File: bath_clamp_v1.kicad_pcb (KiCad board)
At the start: 6 copper layers, 70.9 x 62 mm, 31 parts, among them J1 105-1103-001, J2 105-1103-001, K1 1462042-8, K2 1462042-8, Q1 MBT3904DW1T1G, Q2 MBT3904DW1T1G, Q3 MBT3904DW1T1G, U1 OPA828, U17 MAX5802, U2 ADG1208, U3 G6L-1F-TR-DC5, U4 G6L-1F-TR-DC5, U5 G6L-1F-TR-DC5

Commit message: updates to pcb layout
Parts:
- removed C52, C53: 0.1u, bath_clamp_v1:C0603
- removed H2, H4: MOUNT-HOLE3.0, bath_clamp_v1:3,0
- removed Q2: MBT3904DW1T1G, digikey-footprints:SOT-363
- removed U$1, U$2: HDMI, bath_clamp_v1:HDMI_A
- added C10: 200pF, Capacitor_SMD:C_0603_1608Metric, F.Cu at (113.0, 73.0)
- added C11: 1nF, Capacitor_SMD:C_0603_1608Metric, F.Cu at (113.0, 73.0)
- added C12: 4.7nF, Capacitor_SMD:C_0603_1608Metric, F.Cu at (113.0, 73.0)
- added C13: 0.1u, Capacitor_SMD:C_0603_1608Metric, F.Cu at (62.0, 74.0)
- added C14, C18, C5, C7: 0.1u, Capacitor_SMD:C_0603_1608Metric, F.Cu at (113.0, 73.0)
- added C15: 4.7u, Capacitor_SMD:C_1206_3216Metric, F.Cu at (52.0, 74.0)
- added C16: 4.7u, Capacitor_SMD:C_1206_3216Metric, F.Cu at (61.0, 66.0)
- added C17: 0.1u, Capacitor_SMD:C_0603_1608Metric, F.Cu at (56.0, 59.0)
- added C19: 2.2u, Capacitor_SMD:C_0603_1608Metric, F.Cu at (113.0, 73.0)
- added C2: 0.1u, Capacitor_SMD:C_0603_1608Metric, F.Cu at (47.0, 74.0)
- added C20: 0.1u, Capacitor_SMD:C_0603_1608Metric, F.Cu at (107.0, 8.00)
- added C21: 0.1u, Capacitor_SMD:C_0603_1608Metric, F.Cu at (51.0, 59.0)
- added C22: 0.1u, Capacitor_SMD:C_0603_1608Metric, F.Cu at (57.0, 74.0)
- added C23: DNI, Capacitor_SMD:C_0603_1608Metric, F.Cu at (119.0, 13.0)
- added C24: DNI, Capacitor_SMD:C_0603_1608Metric, F.Cu at (113.0, 73.0)
- added C25: DNI, Capacitor_SMD:C_0603_1608Metric, F.Cu at (124.0, 10.0)
- added C26: DNI, Capacitor_SMD:C_0603_1608Metric, F.Cu at (119.0, 9.00)
- added C3: 1u, Capacitor_SMD:C_0603_1608Metric, F.Cu at (42.0, 74.0)
- added C4: 0.1u, Capacitor_SMD:C_0603_1608Metric, F.Cu at (112.0, 8.00)
- added C6: 4.7n, Capacitor_SMD:C_0603_1608Metric, F.Cu at (113.0, 73.0)
- added C8: 0.1u, Capacitor_SMD:C_0603_1608Metric, F.Cu at (61.0, 59.0)
- added C9: 47pF, Capacitor_SMD:C_0603_1608Metric, F.Cu at (113.0, 73.0)
- added H5: MountingHole_Pad, MountingHole:MountingHole_3.2mm_M3_DIN965_Pad, F.Cu at (55.0, 66.0)
- added H7: MountingHole_Pad, MountingHole:MountingHole_3.2mm_M3_DIN965_Pad, F.Cu at (92.0, 17.0)
- added IC1: DAC53401DSGR, covg-kicad:SON50P200X200X80-9N, F.Cu at (124.0, 37.0)
- added J3: 105-1103-001, digikey-footprints:Test_Jack_Horiz, F.Cu at (123.0, 25.0)
- added Q4: MBT3904DW1T1G, digikey-footprints:SOT-363, F.Cu at (112.0, 26.0)
- added R1, R23, R26: 0, Resistor_SMD:R_0603_1608Metric, F.Cu at (113.0, 73.0)
- added R10, R11, R12, R13, R19, R2, R22, R27, R31, R38, R50, R9: 10k, Resistor_SMD:R_0603_1608Metric, F.Cu at (113.0, 73.0)
- added R14, R15, R16: 240, Resistor_SMD:R_0603_1608Metric, F.Cu at (113.0, 73.0)
- added R17: 1.13k, Resistor_SMD:R_0603_1608Metric, F.Cu at (113.0, 73.0)
- added R18, R24, R44, R45: 33, Resistor_SMD:R_0603_1608Metric, F.Cu at (113.0, 73.0)
- added R20: 73.2k, Resistor_SMD:R_0603_1608Metric, F.Cu at (45.0, 66.0)
- added R21: 73.2k, Resistor_SMD:R_0603_1608Metric, F.Cu at (45.0, 70.0)
- added R25, R30: 20k, Resistor_SMD:R_0603_1608Metric, F.Cu at (113.0, 73.0)
- added R28, R29: 73.2k, Resistor_SMD:R_0603_1608Metric, F.Cu at (113.0, 73.0)
- added R3, R47: 33.2k, Resistor_SMD:R_0603_1608Metric, F.Cu at (113.0, 73.0)
- added R32: 12.1k, Resistor_SMD:R_0603_1608Metric, F.Cu at (113.0, 73.0)
- added R37: 2.49k, Resistor_SMD:R_0603_1608Metric, F.Cu at (113.0, 73.0)
- added R39, R40: 1820, Resistor_SMD:R_0603_1608Metric, F.Cu at (113.0, 73.0)
- added R4: 100k, Resistor_SMD:R_0603_1608Metric, F.Cu at (113.0, 73.0)
- added R41: 1k, Resistor_SMD:R_0603_1608Metric, F.Cu at (113.0, 73.0)
- added R42, R43: 499, Resistor_SMD:R_0603_1608Metric, F.Cu at (113.0, 73.0)
- added R46: 3.01k, Resistor_SMD:R_0603_1608Metric, F.Cu at (113.0, 73.0)
- added R48: 27.4k, Resistor_SMD:R_0603_1608Metric, F.Cu at (113.0, 73.0)
- added R49: 3.01k, Resistor_SMD:R_0603_1608Metric, F.Cu at (124.0, 14.0)
- added R5: 332k, Resistor_SMD:R_0603_1608Metric, F.Cu at (113.0, 73.0)
- added R51: DNI, Resistor_SMD:R_0603_1608Metric, F.Cu at (113.0, 73.0)
- added R6: 1M, Resistor_SMD:R_0603_1608Metric, F.Cu at (113.0, 73.0)
- added R7: 3.32M, Resistor_SMD:R_0603_1608Metric, F.Cu at (113.0, 73.0)
- added R8: 10M, Resistor_SMD:R_0603_1608Metric, F.Cu at (113.0, 73.0)
- added U10: LP2951-3.3_SOIC, Package_SO:SOIC-8_3.9x4.9mm_P1.27mm, F.Cu at (81.0, 64.0)
- added U11: AD8615, Package_TO_SOT_SMD:TSOT-23-5, F.Cu at (124.0, 42.0)
- added U12: TCA9555DBR, Package_SO:SSOP-24_5.3x8.2mm_P0.65mm, F.Cu at (113.0, 63.0)
- added U13: TCA9555DBR, Package_SO:SSOP-24_5.3x8.2mm_P0.65mm, F.Cu at (116.0, 51.0)
- added U14: DG412xUE, Package_SO:TSSOP-16_4.4x5mm_P0.65mm, F.Cu at (117.0, 41.0)
- added U15: OPA828, Package_SO:SOIC-8_3.9x4.9mm_P1.27mm, F.Cu at (113.0, 73.0)
- added U16: TMUX6111PWR, Package_SO:TSSOP-16_4.4x5mm_P0.65mm, F.Cu at (92.0, 70.0)
- added U18: AD8421ARZ, digikey-footprints:TSSOP-8_W3mm, F.Cu at (70.0, 65.0)
- added U19: ADA4932-1YCPZ-R7, digikey-footprints:VFQFN-16-1EP_3x3mm, F.Cu at (83.0, 72.0)
- added U20: TMUX6111PWR, Package_SO:TSSOP-16_4.4x5mm_P0.65mm, F.Cu at (92.0, 62.0)
- added U21: TMUX6111PWR, Package_SO:TSSOP-16_4.4x5mm_P0.65mm, F.Cu at (73.9, 39.4)
- added U22: HDMI, bath_clamp_v1:HDMI_A, F.Cu at (5.08, 29.5)
- added U23: OPA188xxDBV, Package_TO_SOT_SMD:TSOT-23-5, F.Cu at (124.0, 48.0)
- added U6: 24AA025UID, Package_SO:SOIC-8_3.9x4.9mm_P1.27mm, F.Cu at (116.0, 33.0)
- added U7: LM337L_SO8, Package_SO:SOIC-8_3.9x4.9mm_P1.27mm, F.Cu at (113.0, 73.0)
- added U8: AD8615, Package_TO_SOT_SMD:TSOT-23-5, F.Cu at (124.0, 54.0)
- added U9: MCP1804x-3302xOT, Package_TO_SOT_SMD:SOT-23-5, F.Cu at (124.0, 32.0)
- D1, D2, D3, D4, D5: value D -> 1N4007; footprint Diode_SMD:D_SOD-323 -> Diode_SMD:D_SOD-123F
- H1, H3: value MOUNT-HOLE3.0 -> MountingHole_Pad; footprint bath_clamp_v1:3,0 -> MountingHole:MountingHole_3.2mm_M3_DIN965_Pad
- R33: value 4.7k -> 30.1k; footprint bath_clamp_v1:R0603 -> Resistor_SMD:R_0603_1608Metric
- R34: value 4.7k -> 60.4k; footprint bath_clamp_v1:R0603 -> Resistor_SMD:R_0603_1608Metric
- R35: value 100k -> 200; footprint bath_clamp_v1:R0603 -> Resistor_SMD:R_0603_1608Metric; moved to F.Cu
- R36: value 100k -> 1.1k; footprint bath_clamp_v1:R0603 -> Resistor_SMD:R_0603_1608Metric; moved to F.Cu
- U17: value MAX5802 -> DG412xUE; footprint bath_clamp_v1:21-0061L_MXM -> Package_SO:TSSOP-16_4.4x5mm_P0.65mm
- moved J1 128.6 mm to (93.0, 25.0)
- moved J2 123.3 mm to (63.0, 52.0)
- moved Q1 115.4 mm to (113.0, 19.0)
- moved H1 115.1 mm to (103.0, 17.0)
- moved Q3 113.3 mm to (104.0, 25.0)
- moved U5 113.2 mm to (75.0, 53.0)
- moved D1 109.3 mm to (81.0, 31.0)
- moved K2 102.9 mm to (92.0, 39.0)
- moved H3 100.7 mm to (101.0, 8.00)
- moved K1 82.6 mm to (103.0, 34.0)
- moved U3 78.1 mm to (105.0, 50.0)
- moved U1 76.1 mm to (70.0, 73.0)
- moved U4 75.2 mm to (91.0, 52.0)
- moved D4 66.2 mm to (84.0, 26.0)
- moved R33 62.5 mm to (113.0, 73.0)
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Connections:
- C1 pad 2: Net-(C1-Pad2) -> /bath_clamp_v1_1/compensation_switching/OUT
- K1 pad 3: Net-(C1-Pad2) -> Net-(J2-Pad1)
- K1 pad 7: Net-(J2-Pad1) -> /bath_clamp_v1_1/feedback_buffer/IN
- K2 pad 3: /bath_clamp_v1_1/P2 -> Net-(J1-Pad1)
- K2 pad 7: Net-(J1-Pad1) -> /bath_clamp_v1_1/P2
- Q1 pad 1: Net-(Q1-Pad1) -> GND
- Q1 pad 2: Net-(Q1-Pad2) -> GND
- Q1 pad 6: Net-(Q1-Pad6) -> GND
- R33 pad 1: /bath_clamp_v1_2/DS_SDA -> Net-(C23-Pad1)
- R33 pad 2: 3V3 -> Net-(C25-Pad2)
- R34 pad 1: /bath_clamp_v1_2/DS_SCL -> Net-(C23-Pad1)
- R34 pad 2: 3V3 -> Net-(C26-Pad2)
- R35 pad 1: /bath_clamp_v1_2/DS_CLRB -> Net-(R35-Pad1)
- R35 pad 2: 3V3 -> Net-(R35-Pad2)
- R36 pad 1: GND -> Net-(R35-Pad1)
- U1 pad 2: Net-(C1-Pad2) -> /bath_clamp_v1_1/compensation_switching/OUT
- U1 pad 3: /bath_clamp_v1_1/CMD_bath -> Net-(R26-Pad1)
- U17 pad 1: /bath_clamp_v1_2/5V_REF -> /bath_clamp_v1_1/G4
- U17 pad 10: /bath_clamp_v1_2/DS_CLRB -> Net-(U17-Pad10)
- U17 pad 2: /bath_clamp_v1_2/DS_OUT0 -> Net-(U17-Pad10)
- U17 pad 3: /bath_clamp_v1_2/DS_OUT1 -> Net-(R35-Pad2)
- U17 pad 4: GND -> -15V
- U17 pad 5: 5V -> GND
- U17 pad 6: Net-(R36-Pad2) -> Net-(U17-Pad10)
- U17 pad 7: /bath_clamp_v1_2/DS_SCL -> Net-(R36-Pad2)
- U17 pad 8: /bath_clamp_v1_2/DS_SDA -> /bath_clamp_v1_1/G3
- U17 pad 9: 3V3 -> /bath_clamp_v1_1/G1
- U3 pad 4: Net-(C1-Pad2) -> /bath_clamp_v1_1/feedback_buffer/IN
- U4 pad 2: /bath_clamp_v1_1/P2_CAL_SIG -> /bath_clamp_v1_1/CAL_SIG2
- U5 pad 4: /bath_clamp_v1_1/P1_CAL_SIG -> /bath_clamp_v1_1/CAL_SIG1
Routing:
- net /bath_clamp_v1_2/DS_OUT0: track 37.9 -> 0.00 mm, vias 2 -> 0
- net Net-(J1-Pad1): track 19.7 -> 0.00 mm
- net GND: track 15.1 -> 0.00 mm, vias 3 -> 0
- net Net-(R29-Pad2): track 9.56 -> 0.00 mm, vias 1 -> 0
- net Net-(R36-Pad2): track 7.55 -> 0.00 mm, vias 1 -> 0
- net /bath_clamp_v1_3/AMP_PWR+: track 7.44 -> 0.00 mm
- net /bath_clamp_v1_2/DS_CLRB: track 7.29 -> 0.00 mm, vias 1 -> 0
- net Net-(R27-Pad2): track 7.01 -> 0.00 mm, vias 2 -> 0
- net /bath_clamp_v1_3/18V_IN: track 6.06 -> 0.00 mm, vias 1 -> 0
- net 3V3: track 5.70 -> 0.00 mm, vias 2 -> 0
- net /bath_clamp_v1_2/5V_REF: track 4.89 -> 0.00 mm, vias 1 -> 0
- net 5V: track 4.33 -> 0.00 mm, vias 2 -> 0
- net /bath_clamp_v1_3/+15V: track 3.74 -> 0.00 mm, vias 2 -> 0
- net /bath_clamp_v1_2/DS_SDA: track 3.62 -> 0.00 mm
- net /bath_clamp_v1_2/DS_SCL: track 3.19 -> 0.00 mm
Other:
- board size 70.9 x 62 mm -> 127 x 76.2 mm
- net class Default: clearance 0.127 -> 0.1524; trace_width 0.25 -> 0.1524; via_dia 0.8 -> 0.4064; via_drill 0.4 -> 0.254
- rule pad_to_mask_clearance: 0 -> 0.0508
- rule trace_clearance: 0.127 -> 0.1524
- rule trace_min: 0.127 -> 0.1524
- rule via_min_drill: 0.2032 -> 0.254
- rule via_min_size: 0.4 -> 0.4064
- board text removed: "+15V"
- board text removed: "3V3"
- board text removed: "A_PWR+"
- board text removed: "A_PWR-"

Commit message: made sheet for Howland
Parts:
- added C27: DNI, Capacitor_SMD:C_0603_1608Metric, F.Cu at (56.2, 11.7)
- added C28: DNI, Capacitor_SMD:C_0603_1608Metric, F.Cu at (61.3, 5.07)
- added C29: 0.1u, Capacitor_SMD:C_0603_1608Metric, F.Cu at (56.2, 14.2)
- added C30: 0.1u, Capacitor_SMD:C_0603_1608Metric, F.Cu at (61.3, 7.58)
- added C31: 0.1u, Capacitor_SMD:C_0603_1608Metric, F.Cu at (60.2, 10.1)
- added C32: 0.1u, Capacitor_SMD:C_0603_1608Metric, F.Cu at (65.3, 5.07)
- added C33: 5p, Capacitor_SMD:C_0603_1608Metric, F.Cu at (60.2, 12.6)
- added C34: 0.1u, Capacitor_SMD:C_0603_1608Metric, F.Cu at (65.3, 7.58)
- added C35: 0.1u, Capacitor_SMD:C_0603_1608Metric, F.Cu at (64.2, 10.1)
- added J4: HDMI_A, bath_clamp_v1:HDMI_A, F.Cu at (5.59, 20.1)
- added R52: 1M, Resistor_SMD:R_0603_1608Metric, F.Cu at (64.2, 15.1)
- added R53: 1M, Resistor_SMD:R_0603_1608Metric, F.Cu at (68.2, 12.6)
- added R54: 1M, Resistor_SMD:R_0603_1608Metric, F.Cu at (68.2, 15.1)
- added R55: DNI, Resistor_SMD:R_0603_1608Metric, F.Cu at (75.5, 11.7)
- added R56: 10k, Resistor_SMD:R_0603_1608Metric, F.Cu at (79.5, 11.7)
- added R57: 33, Resistor_SMD:R_0603_1608Metric, F.Cu at (83.5, 11.7)
- added R58: 120, Resistor_SMD:R_0603_1608Metric, F.Cu at (87.6, 11.7)
- added U24: LMP8350MA_NOPB, covg-kicad:LMP8350MA&slash_NOPB, F.Cu at (87.9, 4.83)
- C23: value DNI -> 70p
- C24: value DNI -> 20p
- C25: value DNI -> 8p
- C26: value DNI -> 4p
- R19: value 10k -> 20k
- R20: value 73.2k -> 0
- R21: value 73.2k -> 2k
- R27: value 10k -> 0
- R28: value 73.2k -> 1M
- R29: value 73.2k -> DNI
- U11: value AD8615 -> OPA991S; footprint Package_TO_SOT_SMD:TSOT-23-5 -> Package_TO_SOT_SMD:SOT-23-6
- U19: value ADA4932-1YCPZ-R7 -> TMUX6136PWR; footprint digikey-footprints:VFQFN-16-1EP_3x3mm -> Package_SO:TSSOP-16_4.4x5mm_P0.65mm
- U22: value HDMI -> TMUX6136PWR; footprint bath_clamp_v1:HDMI_A -> Package_SO:TSSOP-16_4.4x5mm_P0.65mm
- U8: value AD8615 -> OPA2156xD; footprint Package_TO_SOT_SMD:TSOT-23-5 -> Package_SO:SOIC-8_3.9x4.9mm_P1.27mm
- moved U9 104.8 mm to (21.6, 54.4)
- moved U6 104.2 mm to (16.3, 63.2)
- moved C4 98.3 mm to (26.4, 56.4)
- moved H7 89.2 mm to (3.56, 5.08)
- moved C5 88.8 mm to (26.4, 53.1)
- moved U8 84.3 mm to (50.0, 13.6)
- moved R1 78.4 mm to (60.2, 15.1)
- moved R28 77.2 mm to (68.2, 10.1)
- moved U11 76.1 mm to (56.9, 6.14)
- moved U7 75.6 mm to (38.1, 62.7)
- moved U19 72.7 mm to (50.1, 7.11)
- moved U2 68.2 mm to (71.6, 24.1)
- moved J2 62.2 mm to (123.7, 38.6)
- moved H1 57.9 mm to (122.2, 71.6)
- moved R20 56.7 mm to (64.2, 12.6)
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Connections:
- C1 pad 1: /bath_clamp_v1_1/AMP_OUT -> /bath_clamp_v1_1/RF_1
- R1 pad 1: /bath_clamp_v1_1/AMP_OUT -> Net-(R1-Pad1)
- R1 pad 2: Net-(R1-Pad2) -> /bath_clamp_v1_1/P1_BUF
- R19 pad 2: Net-(R19-Pad2) -> Net-(C27-Pad1)
- R2 pad 1: /bath_clamp_v1_1/AMP_OUT -> /bath_clamp_v1_1/RF_1
- R20 pad 1: Net-(R19-Pad2) -> Net-(R20-Pad1)
- R20 pad 2: /bath_clamp_v1_1/compensation_switching/IN -> Net-(R20-Pad2)
- R21 pad 1: Net-(R19-Pad2) -> Net-(C27-Pad1)
- R21 pad 2: -15V -> GND
- R24 pad 1: Net-(R24-Pad1) -> /bath_clamp_v1_1/CAL_ADC
- R24 pad 2: Net-(R24-Pad2) -> Net-(C28-Pad2)
- R27 pad 1: Net-(R24-Pad2) -> Net-(C28-Pad2)
- R27 pad 2: Net-(R27-Pad2) -> Net-(C28-Pad1)
- R28 pad 1: Net-(R27-Pad2) -> Net-(C33-Pad1)
- R28 pad 2: Net-(R28-Pad2) -> GND
- R29 pad 1: Net-(R27-Pad2) -> Net-(C28-Pad1)
- R29 pad 2: -15V -> GND
- R3 pad 1: /bath_clamp_v1_1/AMP_OUT -> /bath_clamp_v1_1/RF_1
- R39 pad 2: /bath_clamp_v1_1/adc_driver/IOUT -> Net-(R39-Pad2)
- R4 pad 1: /bath_clamp_v1_1/AMP_OUT -> /bath_clamp_v1_1/RF_1
- R40 pad 2: GND -> Net-(R40-Pad2)
- R42 pad 2: Net-(R39-Pad1) -> Net-(R40-Pad2)
- R43 pad 1: Net-(R40-Pad1) -> Net-(R39-Pad1)
- R44 pad 1: Net-(R44-Pad1) -> Net-(R42-Pad1)
- R45 pad 1: Net-(R45-Pad1) -> Net-(R43-Pad2)
- R5 pad 1: /bath_clamp_v1_1/AMP_OUT -> /bath_clamp_v1_1/RF_1
- R6 pad 1: /bath_clamp_v1_1/AMP_OUT -> /bath_clamp_v1_1/RF_1
- R7 pad 1: /bath_clamp_v1_1/AMP_OUT -> /bath_clamp_v1_1/RF_1
- R8 pad 1: /bath_clamp_v1_1/AMP_OUT -> /bath_clamp_v1_1/RF_1
- U1 pad 6: /bath_clamp_v1_1/AMP_OUT -> /bath_clamp_v1_1/RF_1
- U11 pad 1: Net-(R24-Pad2) -> Net-(C33-Pad2)
- U11 pad 2: GND -> -15V
- U11 pad 3: GND -> Net-(R52-Pad1)
- U11 pad 4: Net-(R27-Pad2) -> Net-(C33-Pad1)
- U11 pad 5: +5V -> /bath_clamp_v1_1/H_SDOWN
- U12 pad 20: /bath_clamp_v1_1/G4 -> /bath_clamp_v1_1/FDBK
- U13 pad 17: Net-(U13-Pad17) -> /bath_clamp_v1_1/S1
- U13 pad 18: Net-(U13-Pad18) -> /bath_clamp_v1_1/S2
- U13 pad 19: Net-(U13-Pad19) -> /bath_clamp_v1_1/H_SDOWN
- U13 pad 20: Net-(U13-Pad20) -> /bath_clamp_v1_1/RF_1_OUT
- U14 pad 10: /bath_clamp_v1_1/compensation_switching/IN -> /bath_clamp_v1_1/P1_BUF
- U14 pad 15: /bath_clamp_v1_1/compensation_switching/IN -> /bath_clamp_v1_1/P1_BUF
- U14 pad 2: /bath_clamp_v1_1/compensation_switching/IN -> /bath_clamp_v1_1/P1_BUF
- U14 pad 6: /bath_clamp_v1_1/compensation_switching/IN -> /bath_clamp_v1_1/P1_BUF
- U15 pad 6: /bath_clamp_v1_1/compensation_switching/IN -> /bath_clamp_v1_1/P1_BUF
- U17 pad 1: /bath_clamp_v1_1/G4 -> /bath_clamp_v1_1/adc_driver/G4
- U18 pad 1: /bath_clamp_v1_1/P2 -> Net-(U18-Pad1)
- U18 pad 4: /bath_clamp_v1_1/AMP_OUT -> /bath_clamp_v1_1/P2
- U18 pad 6: /bath_clamp_v1_1/VCM -> GND
- U18 pad 7: /bath_clamp_v1_1/adc_driver/IOUT -> /bath_clamp_v1_1/INAMP_OUT
- U19 pad 1: Net-(R43-Pad2) -> /bath_clamp_v1_1/FDBK
- U19 pad 10: Net-(R44-Pad1) -> /bath_clamp_v1_1/RF_1
- U19 pad 11: Net-(R45-Pad1) -> Net-(R20-Pad2)
- U19 pad 12: Net-(R41-Pad2) -> /bath_clamp_v1_1/CAL_OUT
- U19 pad 13: -2V5 -> +15V
- U19 pad 14: -2V5 -> Net-(U19-Pad14)
- U19 pad 15: -2V5 -> Net-(U19-Pad15)
- U19 pad 16: -2V5 -> Net-(U19-Pad16)
- U19 pad 2: Net-(R39-Pad1) -> /bath_clamp_v1_1/P1_BUF
- U19 pad 3: Net-(R40-Pad1) -> /bath_clamp_v1_1/compensation_switching/IN
- U19 pad 4: Net-(R42-Pad1) -> GND
- U19 pad 5: +7V -> -15V
- U19 pad 6: +7V -> GND
- U19 pad 7: +7V -> Net-(U19-Pad7)
- U19 pad 8: +7V -> Net-(U19-Pad8)
- U19 pad 9: /bath_clamp_v1_1/VCM -> /bath_clamp_v1_1/RF_1_OUT
- U2 pad 4: Net-(R1-Pad2) -> Net-(R52-Pad1)
- U20 pad 11: /bath_clamp_v1_1/CAL_ADC -> /bath_clamp_v1_1/CAL_OUT
- U20 pad 14: /bath_clamp_v1_1/CAL_ADC -> /bath_clamp_v1_1/CAL_OUT
- U20 pad 3: /bath_clamp_v1_1/CAL_ADC -> /bath_clamp_v1_1/CAL_OUT
- U20 pad 6: /bath_clamp_v1_1/CAL_ADC -> /bath_clamp_v1_1/CAL_OUT
- U8 pad 2: GND -> Net-(C27-Pad1)
- U8 pad 3: GND -> Net-(R1-Pad1)
- U8 pad 4: Net-(R19-Pad2) -> -15V
- U8 pad 5: +5V -> Net-(R20-Pad1)

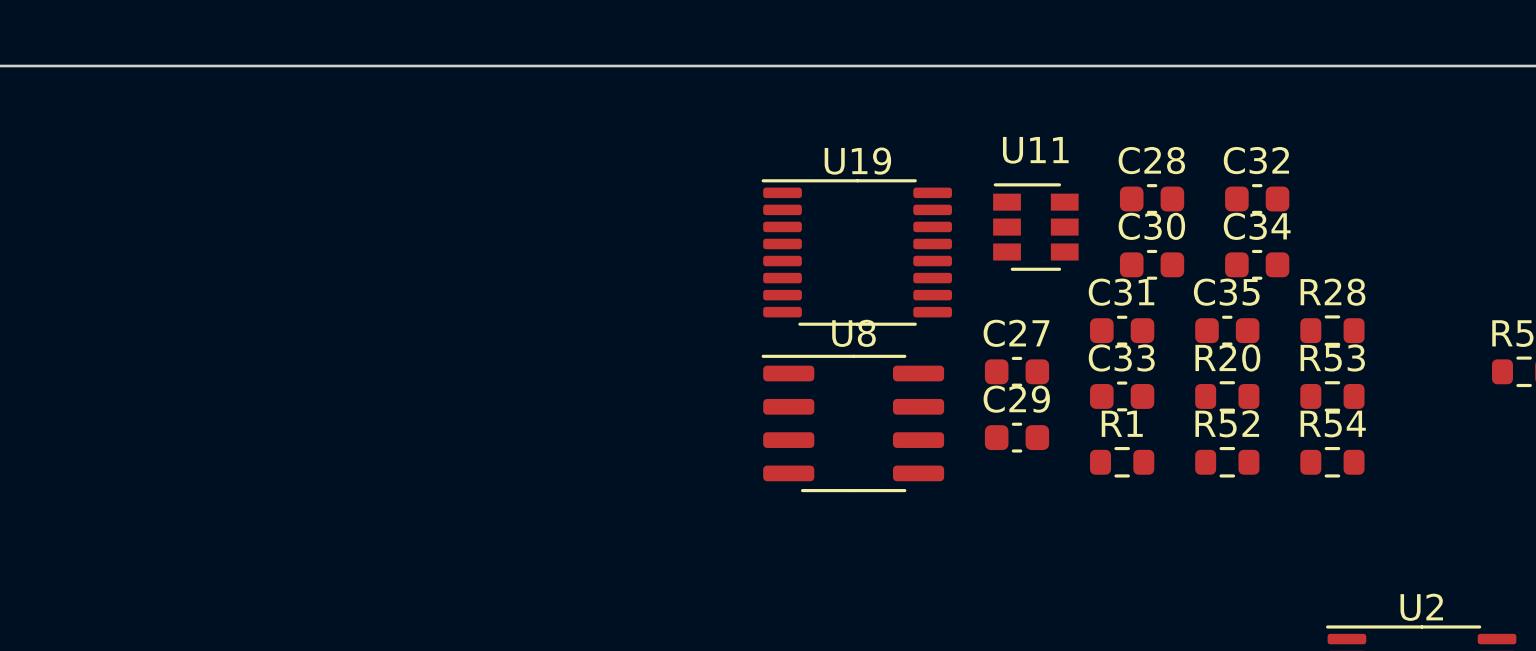
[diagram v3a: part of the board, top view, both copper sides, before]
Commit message: removed all references to clamp footprints
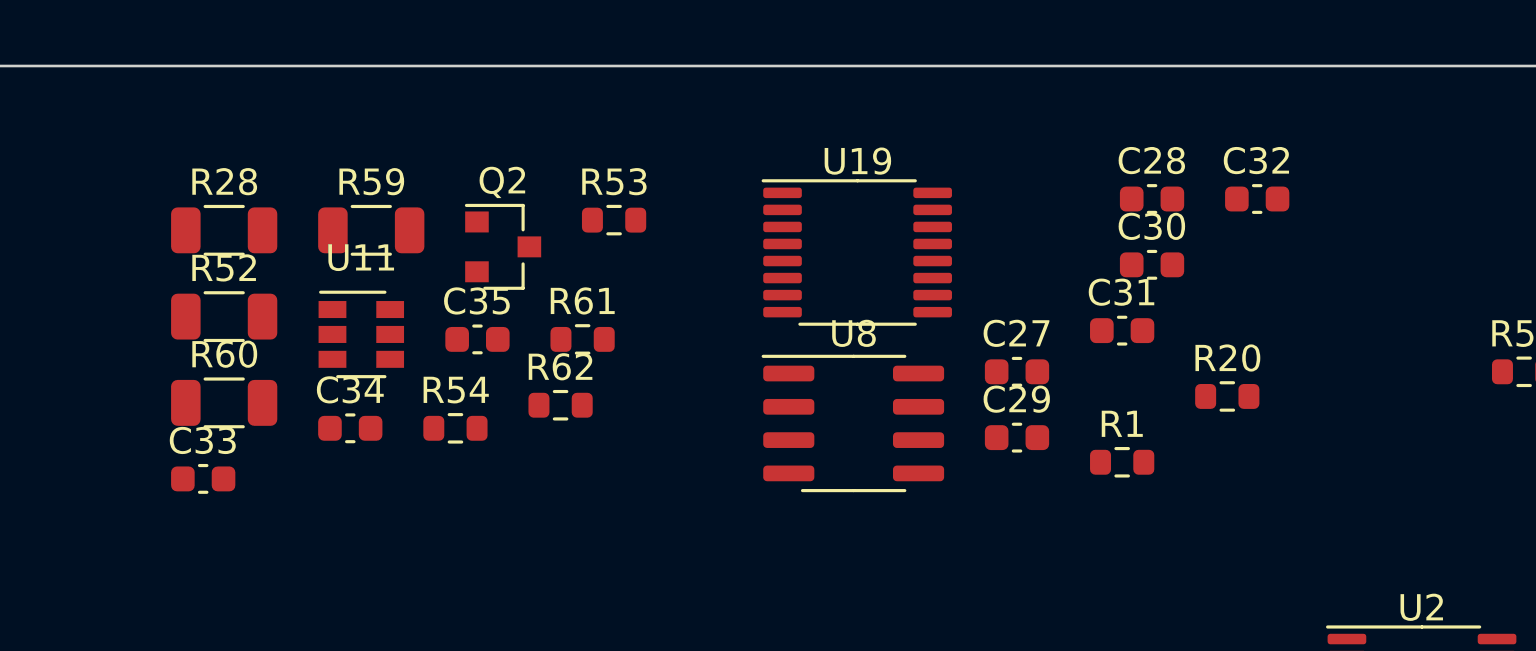
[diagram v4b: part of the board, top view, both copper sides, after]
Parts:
- added Q2: BC856, Package_TO_SOT_SMD:SOT-23, F.Cu at (36.6, 6.90)
- added R59: 4.7M, Resistor_SMD:R_1206_3216Metric, F.Cu at (31.6, 6.27)
- added R60: 4.7M, Resistor_SMD:R_1206_3216Metric, F.Cu at (25.9, 12.8)
- added R61: 470k, Resistor_SMD:R_0603_1608Metric, F.Cu at (39.6, 10.4)
- added R62: 10k, Resistor_SMD:R_0603_1608Metric, F.Cu at (38.8, 12.9)
- J4: footprint bath_clamp_v1:HDMI_A -> covg-kicad:HDMI_A
- R28, R52: value 1M -> 4.7M; footprint Resistor_SMD:R_0603_1608Metric -> Resistor_SMD:R_1206_3216Metric
- R53, R54: value 1M -> 0
- moved R28 42.4 mm to (25.9, 6.27)
- moved R52 38.7 mm to (25.9, 9.56)
- moved C33 35.2 mm to (25.1, 15.7)
- moved C34 35.1 mm to (30.8, 13.8)
- moved R54 33.5 mm to (34.8, 13.8)
- moved C35 28.6 mm to (35.6, 10.4)
- moved R53 28.2 mm to (40.8, 5.88)
- moved U11 26.1 mm to (31.2, 10.2)
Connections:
- R28 pad 1: Net-(C33-Pad1) -> Net-(R28-Pad1)
- R28 pad 2: GND -> /bath_clamp_v1_1/CMD
- R52 pad 2: /bath_clamp_v1_1/CMD -> GND
- R53 pad 1: Net-(C33-Pad2) -> /bath_clamp_v1_1/howland_ipump/I_OUT
- R53 pad 2: Net-(R52-Pad1) -> Net-(R28-Pad1)
- R54 pad 1: Net-(C33-Pad2) -> Net-(C33-Pad1)
- R54 pad 2: Net-(C33-Pad1) -> Net-(R52-Pad1)
- U11 pad 3: Net-(R52-Pad1) -> /bath_clamp_v1_1/howland_ipump/I_OUT
- U11 pad 5: /bath_clamp_v1_1/H_SDOWN -> Net-(Q2-Pad3)
- U13 pad 19: /bath_clamp_v1_1/H_SDOWN -> /bath_clamp_v1_1/EN_IPUMP
- U2 pad 4: Net-(R52-Pad1) -> /bath_clamp_v1_1/howland_ipump/I_OUT

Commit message: layout updates; part positioning
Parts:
- added C36: 0.1u, Capacitor_SMD:C_0603_1608Metric, F.Cu at (15.2, 39.1)
- added C37: DNI, Capacitor_SMD:C_0603_1608Metric, F.Cu at (66.0, 19.0)
- added C38: 0.1u, Capacitor_SMD:C_0603_1608Metric, F.Cu at (23.4, 32.3)
- added R63: 30k, Resistor_SMD:R_0603_1608Metric, F.Cu at (10.7, 35.1)
- added R64: 3k, Resistor_SMD:R_0603_1608Metric, F.Cu at (10.7, 37.8)
- added R65: 0, Resistor_SMD:R_0603_1608Metric, F.Cu at (21.0, 49.0)
- added R66: 0, Resistor_SMD:R_0603_1608Metric, F.Cu at (28.0, 37.0)
- added R67: DNI, Resistor_SMD:R_0603_1608Metric, F.Cu at (15.0, 29.0)
- added R68: 0, Resistor_SMD:R_0603_1608Metric, F.Cu at (23.4, 35.1)
- added R69: DNI, Resistor_SMD:R_0603_1608Metric, F.Cu at (66.0, 23.0)
- added R70: DNI, Resistor_SMD:R_0603_1608Metric, F.Cu at (70.0, 63.0)
- added R71: 0, Resistor_SMD:R_0603_1608Metric, F.Cu at (21.3, 40.4)
- added U25: OPA2156xD, Package_SO:SOIC-8_3.9x4.9mm_P1.27mm, F.Cu at (17.3, 34.3)
- C17, C18, C2, C29, C3, C30, C34, C35, C4, C5, C7: moved to B.Cu
- IC1: footprint covg-kicad:SON50P200X200X80-9N -> covg-kicad:WSON-8-1EP_2x2mm_P0.5mm_EP0.9x1.6mm_posMask
- J4: footprint covg-kicad:HDMI_A -> covg-kicad:CONN_10029449-111RLF_HDMI_A
- U24: footprint covg-kicad:LMP8350MA&slash_NOPB -> Package_SO:SOIC-8_3.9x4.9mm_P1.27mm
- moved R18 114.7 mm to (14.0, 15.0)
- moved R27 110.5 mm to (24.9, 6.35), turned to 270 degrees
- moved R24 110.1 mm to (17.0, 19.0)
- moved R29 109.8 mm to (21.0, 13.0)
- moved R9 106.4 mm to (18.0, 25.0)
- moved R12 105.1 mm to (26.0, 14.0)
- moved R10 103.4 mm to (23.0, 22.0)
- moved U13 102.4 mm to (13.7, 56.6)
- moved R40 98.8 mm to (42.7, 3.56)
- moved R11 98.6 mm to (28.0, 23.0)
- moved R42 96.5 mm to (43.4, 6.10), turned to 90 degrees
- moved R44 95.3 mm to (42.7, 8.64), turned to 180 degrees
- moved R45 93.4 mm to (42.7, 11.6), turned to 180 degrees
- moved C18 90.5 mm to (52.1, 6.10), turned to 270 degrees
- moved R39 89.7 mm to (55.9, 3.81), turned to 180 degrees
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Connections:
- C1 pad 2: /bath_clamp_v1_1/compensation_switching/OUT -> Net-(C1-Pad2)
- H5 pad 1: GND -> Net-(H5-Pad1)
- R25 pad 1: /bath_clamp_v1_1/CMD -> /bath_clamp_v1_1/CMD_BUF
- R28 pad 2: /bath_clamp_v1_1/CMD -> /bath_clamp_v1_1/CMD_BUF
- U4 pad 2: /bath_clamp_v1_1/CAL_SIG2 -> Net-(J2-Pad1)
- U4 pad 4: Net-(J1-Pad1) -> /bath_clamp_v1_1/CAL_SIG1
- U4 pad 5: Net-(D5-Pad2) -> /bath_clamp_v1_1/P1_CAL
- U5 pad 2: Net-(J2-Pad1) -> /bath_clamp_v1_1/CAL_SIG2
- U5 pad 4: /bath_clamp_v1_1/CAL_SIG1 -> Net-(J1-Pad1)
- U5 pad 5: /bath_clamp_v1_1/P1_CAL -> Net-(D5-Pad2)
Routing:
- net Net-(R16-Pad1): track 0.00 -> 5.05 mm
- net +5V: track 4.15 -> 0.00 mm, vias 1 -> 0
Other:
- net class Default: clearance 0.1524 -> 0.15; trace_width 0.1524 -> 0.15; via_dia 0.4064 -> 0.7; via_drill 0.254 -> 0.3
- rule pad_to_mask_clearance: 0.0508 -> 0
- rule trace_clearance: 0.1524 -> 0.15
- rule trace_min: 0.1524 -> 0.1
- rule via_min_drill: 0.254 -> 0.2
- rule via_min_size: 0.4064 -> 0.5
